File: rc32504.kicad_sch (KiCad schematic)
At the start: 63 parts, among them Q2 DMN62D0U-7, T1 TC2-72T+, T2 TC2-72T+, T3 TC2-72T+, T4 TC2-72T+, U4 RC32504A000GNK#BB0

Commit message: Schematic mostly done
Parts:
- removed C25, C27, C28, C30, C31, C33, C34, C36: 100n, Capacitor_SMD:C_0402_1005Metric, symbol Auto_Library_WUT:Yageo CC0402KRX7R8BB104
- added C151: 1u, Capacitor_SMD:C_0402_1005Metric, symbol Auto_Library_WUT:Kemet C0402C105K4PACTU
- added C154: 100n, Capacitor_SMD:C_0402_1005Metric, symbol Auto_Library_WUT:Yageo CC0402KRX7R8BB104
- added C7 (x3): 10u, Capacitor_SMD:C_0603_1608Metric, symbol Auto_Library_WUT:Samsung Electro-Mechanics CL10A106MO8NQNC
- added FB28: 600R, Inductor_SMD:L_0603_1608Metric, symbol Auto_Library_WUT:Murata BLM18AG601SN1D
- added R119: 330R, Resistor_SMD:R_0402_1005Metric, symbol Auto_Library_WUT:KOA Speer RK73H1ETTP3300F
- added R121: 18k, Resistor_SMD:R_0402_1005Metric, symbol Auto_Library_WUT:KOA Speer RK73H1ETTP1802F
- added R123: 22k, Resistor_SMD:R_0402_1005Metric, symbol Auto_Library_WUT:KOA Speer RK73H1ETTP2202F
- added R125: 4k7, Resistor_SMD:R_0402_1005Metric, symbol Auto_Library_WUT:KOA Speer RK73H1ETTP4701F
- added R127: 100R, Resistor_SMD:R_0402_1005Metric, symbol Auto_Library_WUT:KOA Speer RK73H1ETTP1000F
- added U13: LT3045IDD#PBF, Package_DFN_QFN:DFN-10-1EP_3x3mm_P0.5mm_EP1.65x2.38mm_ThermalVias, symbol IC_WUT:LT3045IDD#PBF
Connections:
- net 1v8_VDDA is gone; now on net 1V8_VDDA: C60.1, C61.1, FB14.2
- net 0V: now also C151.2, C154.2, C7.2, C7.2, C7.2, R119.2, R121.2, R125.2, U13.11 (GND), U13.8 (GND)
- net 1V8_PLL: now also C7.1, C7.1, R123.1, U13.10 (OUT), U13.9 (OUTS)
- net at U4.21 (OUT0_N): now also T1.3
- net at T2.1: now also U4.17 (OUT1_N)
- net at T2.3: now also U4.18 (OUT1_P)
- net at U4.20 (OUT0_P): now also T1.1
- net at U4.11 (OUT3_N): now also T4.1
- net at U4.12 (OUT3_P): now also T4.3
- net at U4.14 (OUT2_N): now also T3.1
- net at U4.15 (OUT2_P): now also T3.3
- new net: C151.1, R121.1, U13.7 (SET)
- new net: R119.1, U13.5 (ILIM)
- new net: R127.1, U13.4 (PG)
- new net: R123.2, R125.1, U13.6 (PGFB)
- new net: C7.1, FB28.2, U13.1 (IN), U13.2 (IN), U13.3 (EN/UV)
- new net 5V0_PI: FB28.1
- new net VDD_PG_OD: C154.1, R127.2
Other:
- note added: "Abs max current draw is 373mA Ilim = 150mA / Rlim(kohm) = 150/0.33 = 450mA"
- note added: "Vfb = 0.3V Vpg = 0.3 * (1+22/4.7) = 1.70V"
- note added: "Vout = 100uA * Rset"

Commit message: schematic complete
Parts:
- removed C154, C35: 100n, Capacitor_SMD:C_0402_1005Metric, symbol Auto_Library_WUT:Yageo CC0402KRX7R8BB104
- removed R123: 22k, Resistor_SMD:R_0402_1005Metric, symbol Auto_Library_WUT:KOA Speer RK73H1ETTP2202F
- removed R125: 4k7, Resistor_SMD:R_0402_1005Metric, symbol Auto_Library_WUT:KOA Speer RK73H1ETTP4701F
- removed R127: 100R, Resistor_SMD:R_0402_1005Metric, symbol Auto_Library_WUT:KOA Speer RK73H1ETTP1000F
- removed T3: TC2-72T+, RF_WUT:MiniCircuits_AT1521, symbol Transformer_WUT:Minicircuits_TC2-72T
- added C111, C114, C164, C165, C3: 100n, Capacitor_SMD:C_0402_1005Metric, symbol Auto_Library_WUT:Yageo CC0402KRX7R8BB104
- added T7: TC2-72T+, RF_WUT:MiniCircuits_AT1521, symbol Transformer_WUT:Minicircuits_TC2-72T
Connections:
- net 1v8_VDDREF is gone; now on net 1V8_VDDREF: C57.1, C58.1, FB13.2
- net 0V: now also T1.2, T2.2, T4.2, T7.2, T7.6; no longer C26.1, C29.1, C32.1
- net RF3: now also T4.4
- net RF4: now also T7.4; no longer T4.4
- net at C32.2: now also T2.1
- net RF2_N: now reaches U4.17 (OUT1_N)
- net RF2_N: now also C32.1; no longer T2.1
- net at C29.2: now also T2.3; no longer T2.2
- net RF2_P: now reaches U4.18 (OUT1_P)
- net RF2_P: now also C29.1; no longer T2.3
- net at T4.1: now also C114.2; no longer U4.11 (OUT3_N)
- net at T4.3: now also C111.2; no longer U4.12 (OUT3_P)
- net RF3_N: now reaches U4.14 (OUT2_N)
- net RF3_N: now also C114.1
- net RF3_P: now reaches U4.15 (OUT2_P)
- net RF3_P: now also C111.1
- net at T1.1: now also C26.2; no longer U4.20 (OUT0_P)
- net at T1.3: now also C3.2; no longer U4.21 (OUT0_N)
- net VIN: now reaches U13.6 (PGFB)
- net VIN: now also C7.1, FB28.2, U13.1 (IN), U13.2 (IN), U13.3 (EN/UV)
- new net: C165.2, T7.1
- new net: C164.2, T7.3
- new net RF1_N: C3.1, U4.21 (OUT0_N)
- new net RF1_P: C26.1, U4.20 (OUT0_P)
- new net RF4_N: C165.1, U4.11 (OUT3_N)
- new net RF4_P: C164.1, U4.12 (OUT3_P)
- no-connect marks 0 -> 1
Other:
- note removed: "Vfb = 0.3V Vpg = 0.3 * (1+22/4.7) = 1.70V"
- moved on the sheet: C26, C7

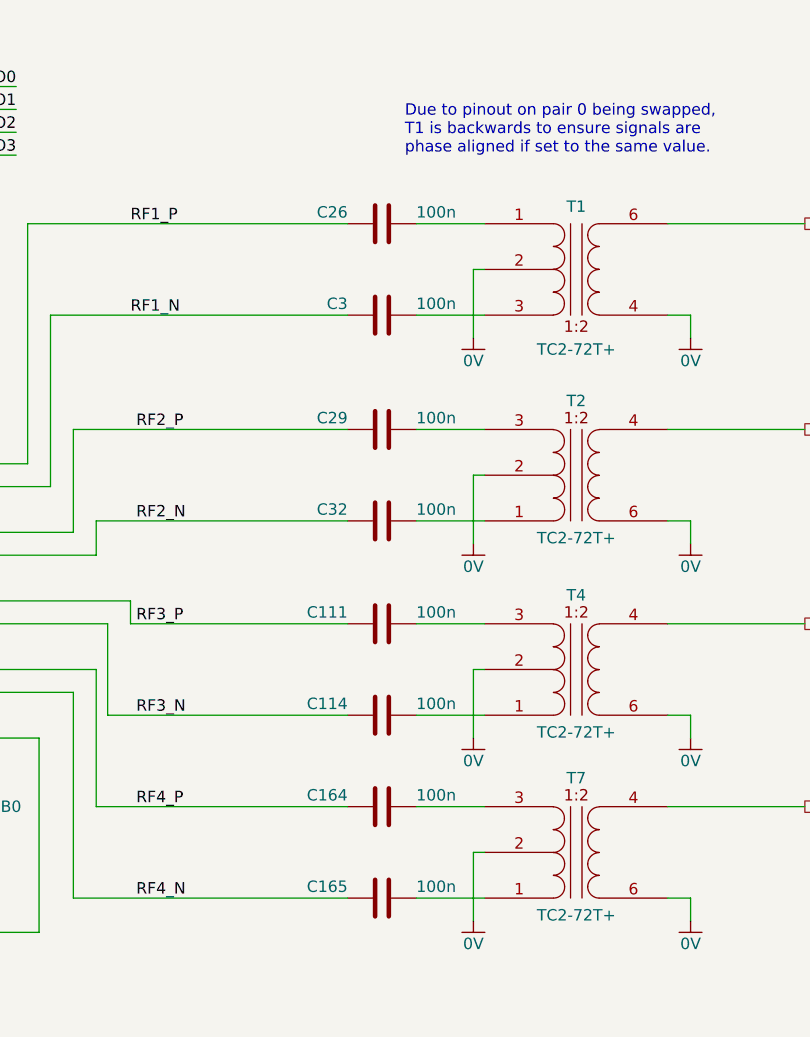
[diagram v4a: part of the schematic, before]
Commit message: Moved to preferred library
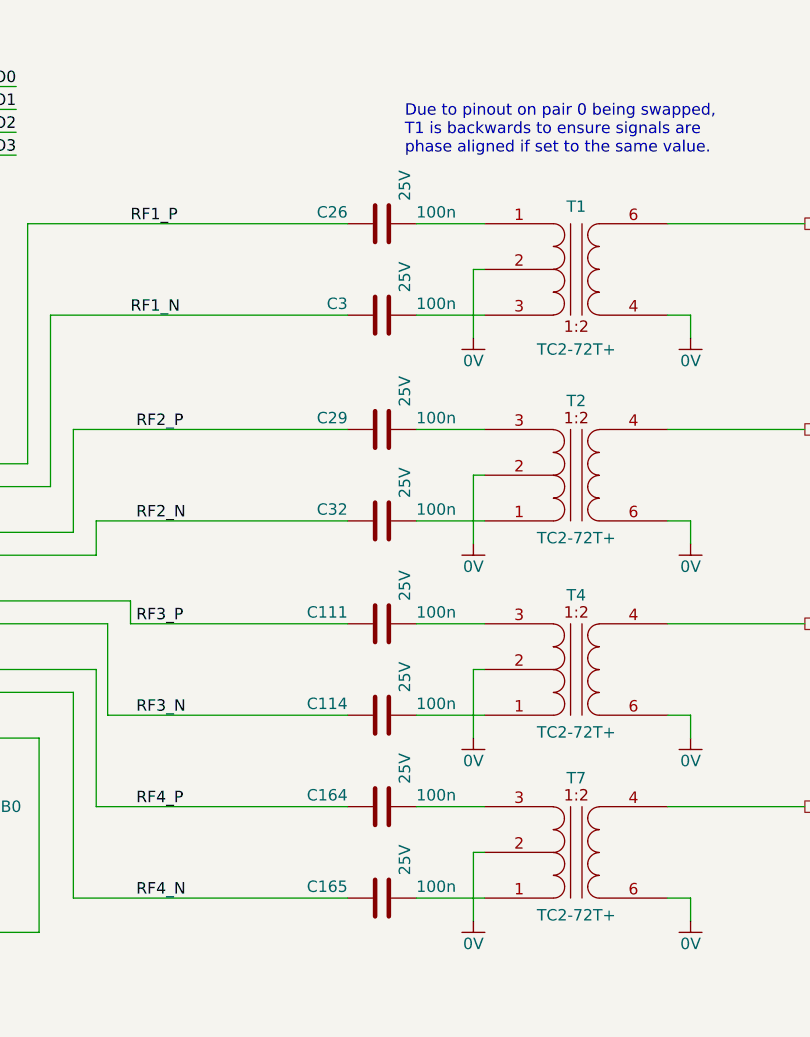
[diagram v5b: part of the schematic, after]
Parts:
- C111, C114, C164, C165, C26, C29, C3, C32, C38, C40, C41, C43, C45, C47, C49, C51, C53, C55, C56, C58, C59, C61, C62, C64, C66: symbol Auto_Library_WUT:Yageo CC0402KRX7R8BB104 -> Preferred_WUT:Yageo CC0402KRX7R8BB104
- C7: symbol Auto_Library_WUT:Samsung Electro-Mechanics CL10A106MO8NQNC -> Preferred_WUT:Samsung Electro-Mechanics CL10A106MO8NQNC
- FB10, FB11, FB12, FB13, FB15, FB8, FB9: symbol Auto_Library_WUT:Murata BLM15BD182SN1D -> Preferred_WUT:Murata BLM15BD182SN1D
- FB14, FB28: symbol Auto_Library_WUT:Murata BLM18AG601SN1D -> Preferred_WUT:Murata BLM18AG601SN1D
- R28: symbol Auto_Library_WUT:KOA Speer RK73H1ETTP1002F -> Preferred_WUT:KOA Speer RK73H1ETTP1002F
- R29, R30: symbol Auto_Library_WUT:KOA Speer RK73H1ETTP1000F -> Preferred_WUT:KOA Speer RK73H1ETTP1000F

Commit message: Started placement
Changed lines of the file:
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@@
-    )
-  )
-  (symbol (lib_id "Power_WUT:PWR_FLAG") (at 105.41 165.1 0) (unit 1)
-    (in_bom yes) (on_board yes) (dnp no) (fields_autoplaced)
-    (property "Reference" "#FLG025" (at 105.41 163.195 0)
-      (effects (font (size 1.27 1.27)) hide)
-    )
-    (property "Value" "PWR_FLAG" (at 105.41 161.29 0)
-      (effects (font (size 1.27 1.27)) hide)
-    )
-    (property "Footprint" "" (at 105.41 165.1 0)
-      (effects (font (size 1.27 1.27)) hide)
-    )
-    (property "Datasheet" "~" (at 105.41 165.1 0)
-      (effects (font (size 1.27 1.27)) hide)
-    )
-    (pin "1")
-    (instances
-      (project "Master Timing Card"
-        (path "/6e8e281e-e30f-459d-852f-231836068db5/4066cd97-f2f5-4d90-9329-88af4fe2410f/1bfa85e8-7bad-4e9e-b685-4f9182ad3688"
-          (reference "#FLG025") (unit 1)
-        )
-        (path "/6e8e281e-e30f-459d-852f-231836068db5/4066cd97-f2f5-4d90-9329-88af4fe2410f/69eeaa75-0bdd-4e0a-b992-8a9cd01c4f2e"
-          (reference "#FLG026") (unit 1)
-        )
-      )
     )
   )

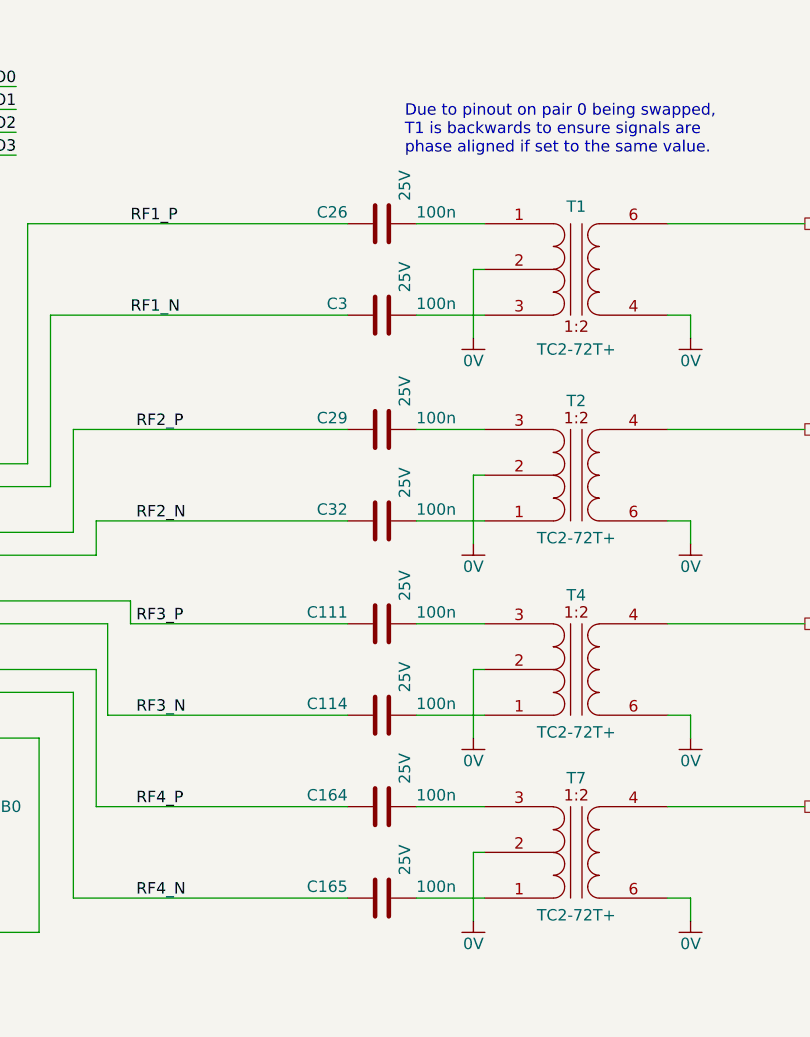
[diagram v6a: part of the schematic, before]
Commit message: moving to discrete GPS recevier
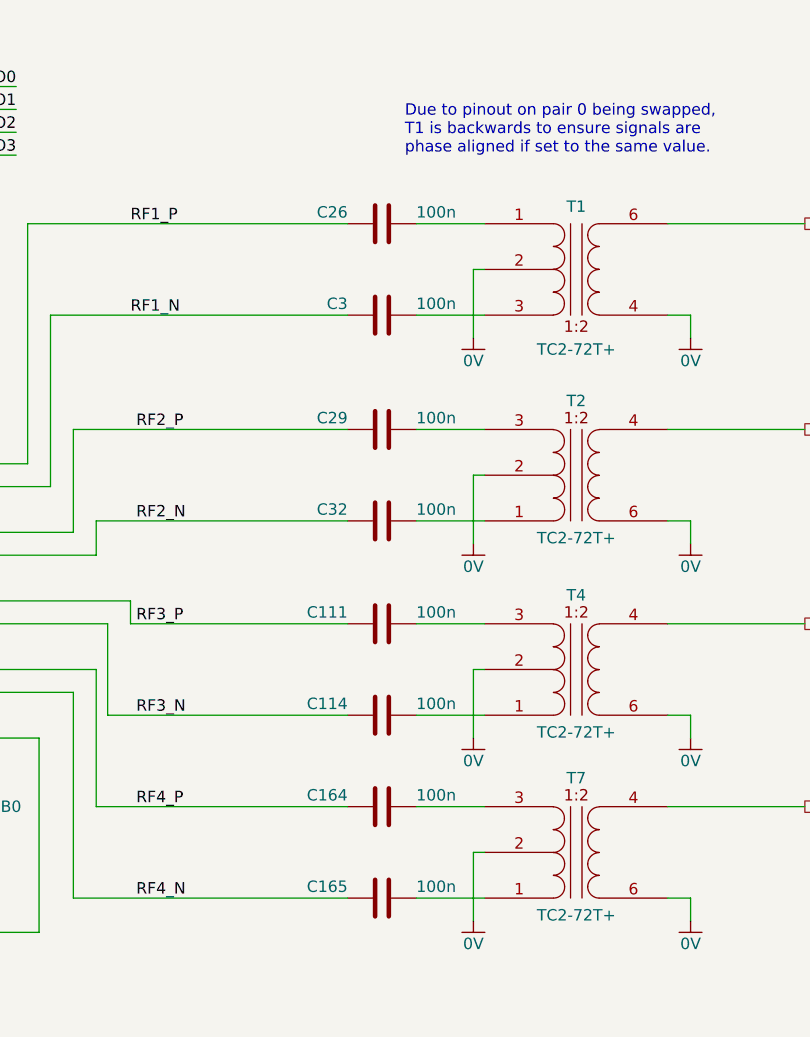
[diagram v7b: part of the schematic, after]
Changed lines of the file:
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@@
     )
     (property "Voltage" "25V" (at 223.52 83.82 0) (do_not_autoplace)
-      (effects (font (size 1.27 1.27) (color 0 100 100 1)) (justify left))
+      (effects (font (size 1.27 1.27) (color 0 100 100 1)) (justify left) hide)
     )
     (property "Manufacturer" "Yageo" (at 220.98 86.36 0)
@@
   )
   (symbol (lib_id "RF_WUT:RC32504A000GNK#BB0") (at 157.48 92.71 0) (unit 1)
-    (in_bom yes) (on_board yes) (dnp no) (fields_autoplaced)
+    (in_bom yes) (on_board yes) (dnp no)
     (property "Reference" "U4" (at 159.6741 138.43 0)
       (effects (font (size 1.27 1.27)) (justify left))
@@
     )
     (property "Voltage" "25V" (at 223.52 148.59 0) (do_not_autoplace)
-      (effects (font (size 1.27 1.27) (color 0 100 100 1)) (justify left))
+      (effects (font (size 1.27 1.27) (color 0 100 100 1)) (justify left) hide)
     )
     (property "Manufacturer" "Yageo" (at 220.98 151.13 0)
@@
     )
     (property "Voltage" "25V" (at 223.52 106.68 0) (do_not_autoplace)
-      (effects (font (size 1.27 1.27) (color 0 100 100 1)) (justify left))
+      (effects (font (size 1.27 1.27) (color 0 100 100 1)) (justify left) hide)
     )
     (property "Manufacturer" "Yageo" (at 220.98 109.22 0)
@@
     )
     (property "Voltage" "25V" (at 223.52 96.52 0) (do_not_autoplace)
-      (effects (font (size 1.27 1.27) (color 0 100 100 1)) (justify left))
+      (effects (font (size 1.27 1.27) (color 0 100 100 1)) (justify left) hide)
     )
     (property "Manufacturer" "Yageo" (at 220.98 99.06 0)
@@
     )
     (property "Voltage" "25V" (at 223.52 138.43 0) (do_not_autoplace)
-      (effects (font (size 1.27 1.27) (color 0 100 100 1)) (justify left))
+      (effects (font (size 1.27 1.27) (color 0 100 100 1)) (justify left) hide)
     )
     (property "Manufacturer" "Yageo" (at 220.98 140.97 0)
@@
     )
     (property "Voltage" "25V" (at 223.52 73.66 0) (do_not_autoplace)
-      (effects (font (size 1.27 1.27) (color 0 100 100 1)) (justify left))
+      (effects (font (size 1.27 1.27) (color 0 100 100 1)) (justify left) hide)
     )
     (property "Manufacturer" "Yageo" (at 220.98 76.2 0)
@@
     )
     (property "Voltage" "25V" (at 223.52 118.11 0) (do_not_autoplace)
-      (effects (font (size 1.27 1.27) (color 0 100 100 1)) (justify left))
+      (effects (font (size 1.27 1.27) (color 0 100 100 1)) (justify left) hide)
     )
     (property "Manufacturer" "Yageo" (at 220.98 120.65 0)
@@
     )
     (property "Voltage" "25V" (at 223.52 128.27 0) (do_not_autoplace)
-      (effects (font (size 1.27 1.27) (color 0 100 100 1)) (justify left))
+      (effects (font (size 1.27 1.27) (color 0 100 100 1)) (justify left) hide)
     )
     (property "Manufacturer" "Yageo" (at 220.98 130.81 0)

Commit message: initial placement
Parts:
- removed C65: 4n7, Capacitor_SMD:C_0402_1005Metric, symbol Auto_Library_WUT:Kemet C0402C472K5RACTU
- removed C66: 100n, Capacitor_SMD:C_0402_1005Metric, symbol Preferred_WUT:Yageo CC0402KRX7R8BB104
- removed Q2: DMN62D0U-7, Package_TO_SOT_SMD:SOT-23, symbol FET_WUT:DMN62D0U-7
- removed R28: 10k, Resistor_SMD:R_0402_1005Metric, symbol Preferred_WUT:KOA Speer RK73H1ETTP1002F
- removed R30: 100R, Resistor_SMD:R_0402_1005Metric, symbol Preferred_WUT:KOA Speer RK73H1ETTP1000F
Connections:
- net ~{PLL_LOCK_OD}: now also R29.2
